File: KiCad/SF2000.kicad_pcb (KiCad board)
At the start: 4 copper layers, 111.5 x 83.9 mm, 104 parts, among them J1 Conn_2Rows-86Pins_even_odd, J10 Conn_02x01, J11 Conn_02x01, J2 Conn_01x02, J20 Conn_02x11_Odd_Even, J3 Conn_02x05_Odd_Even, J4 Conn_02x01, J5 Conn_01x01, J6 Micro_SD_Card_Socket, J7 Conn_02x01, J8 Conn_02x01, J9 Conn_02x01, Q1 MMBT3904, Q2 MMBT3906, U1 LM1117-3.3, U10 IS61WV20488FBLL-10TLI, U11 IS61WV20488FBLL-10TLI, U12 IS61WV20488FBLL-10TLI, U13 IS61WV20488FBLL-10TLI, U14 SST39LF040, U15 SST39LF802C, U16 74AHCT3G14, U2 ABLIC S-1132B43-M5T1U, U20 AT25SF081B-SSH, U3 TLV74312PDBV, U4 SN74CBT16211, U5 SN74CBT16211, U6 SN74CBT16211, U7 SN74AUP1T87DCKR, U8 T8Q144C3, U9 68000D, X1 Oscillator_7.0x5.0mm

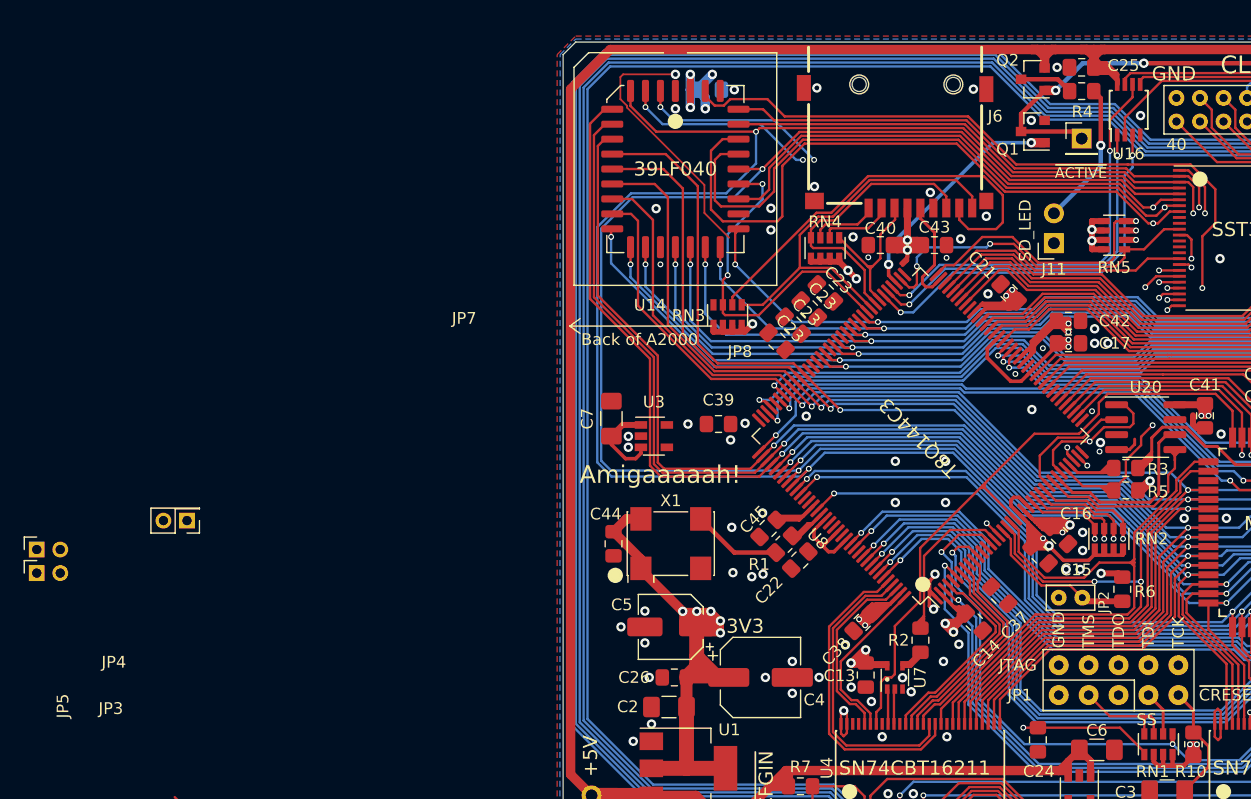
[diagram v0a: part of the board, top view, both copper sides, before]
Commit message: Fixed driver bank select jumper for ROM at U14, pulled-up by vacant resistor in RN3
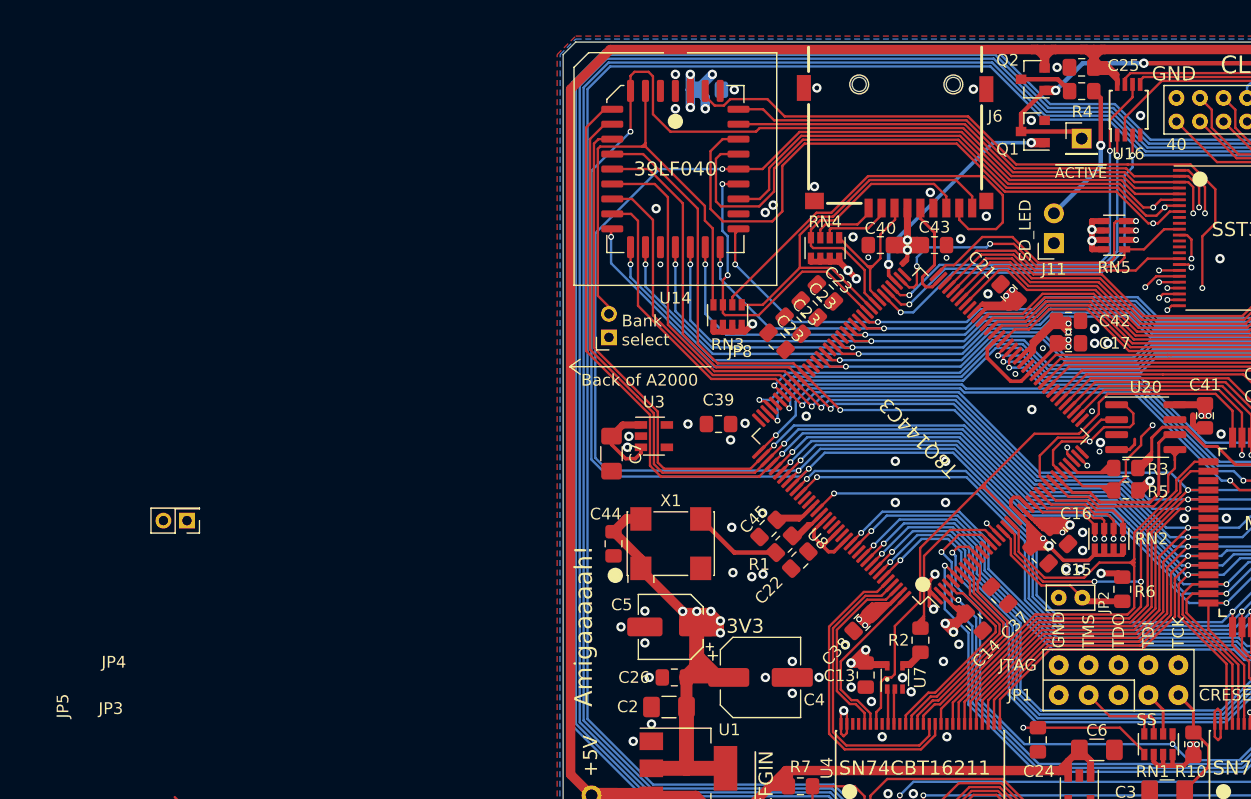
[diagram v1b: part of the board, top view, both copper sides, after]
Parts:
- removed J10: Conn_02x01, Connector_PinHeader_2.00mm:PinHeader_2x01_P2.00mm_Vertical
- moved J9 51.8 mm to (101.5, 84.2), turned to 90 degrees
- moved C7 2.98 mm to (101.8, 94.1), turned to 90 degrees
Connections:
- J9 pad 2: JP7 -> ROM_B1
- RN3 pad 4: Net-(RN3-Pad4) -> ROM_B1
- U14 pad 2: ROM_B2 -> GND
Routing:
- net ROM_B1: track 16.7 -> 39.8 mm, vias 2 -> 0
- net GND: track 152.6 -> 130.4 mm
- net ROM_B2: track 16.4 -> 0.00 mm, vias 2 -> 0
- net A13_3V3: track 253.1 -> 251.0 mm
- net ROM_OE: track 29.5 -> 28.0 mm
- net A12_3V3: track 236.4 -> 235.2 mm
- net A6_3V3: track 210.1 -> 211.2 mm
- net A5_3V3: track 192.5 -> 191.3 mm
- net A4_3V3: track 189.6 -> 188.9 mm
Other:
- board text added: "Bank select"
- board text removed: "JP7"

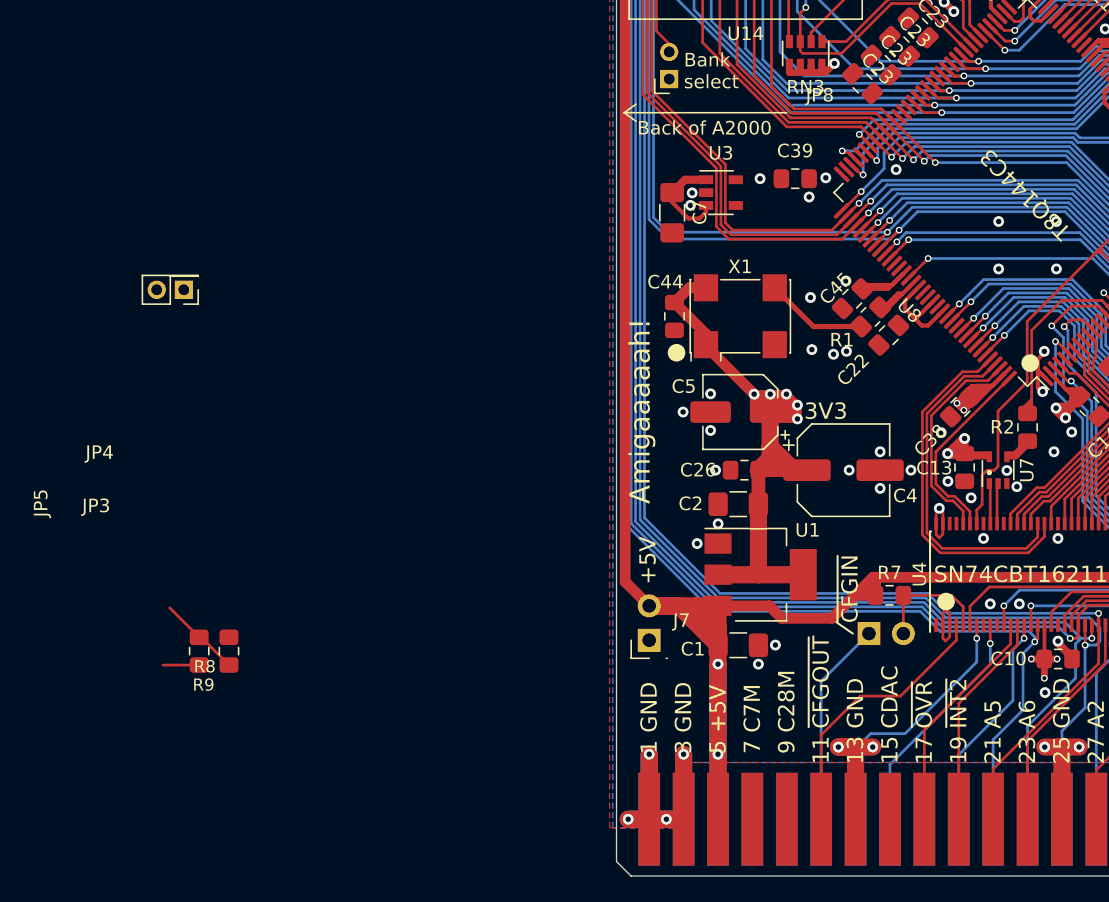
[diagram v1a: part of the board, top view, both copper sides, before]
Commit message: Swap position of BOSS and INT2 signal in FPGA and level shifters
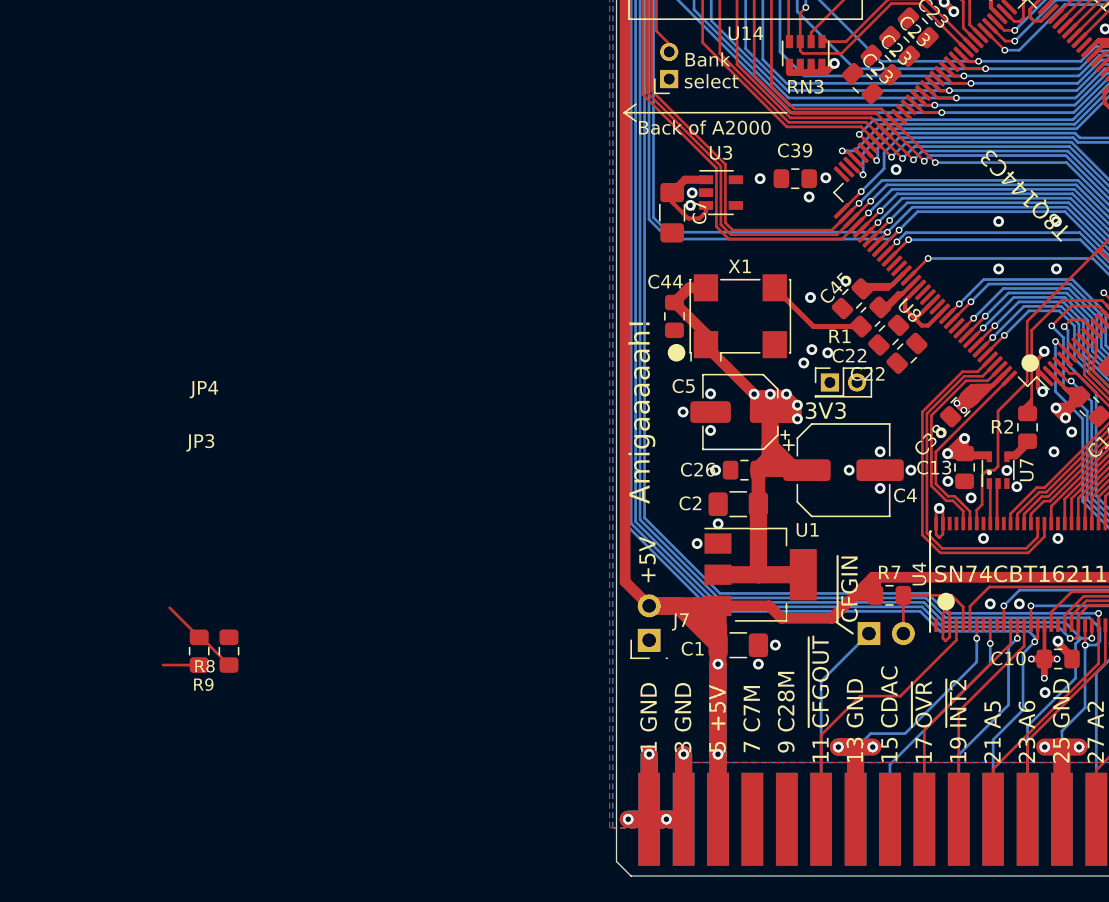
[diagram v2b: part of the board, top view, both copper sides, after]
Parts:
- added C22: 0.1uF, Capacitor_SMD:C_0805_2012Metric_Pad1.15x1.40mm_HandSolder, F.Cu at (119.1, 104.5)
- moved J8 48.2 mm to (113.4, 106.6), turned to 0 degrees
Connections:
- U4 pad 13: INT2 -> BOSS
- U4 pad 14: BOSS -> INT2
- U4 pad 42: BOSS_3V3 -> INT2_3V3
- U4 pad 43: INT2_3V3 -> BOSS_3V3
- U8 pad 10: BOSS_3V3 -> INT2_3V3
- U8 pad 8: INT2_3V3 -> BOSS_3V3
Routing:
- net INT2_3V3: track 17.8 -> 18.5 mm
- net BOSS_3V3: track 18.5 -> 17.8 mm
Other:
- board text removed: "I/O"
- board text removed: "JP5"
- board text removed: "JP8"
- board text removed: "MISO"
- board text removed: "MOSI"
- board text removed: "SCK"
- board text removed: "~CS"
- board text removed: "~INT"
- board text removed: "~RST"

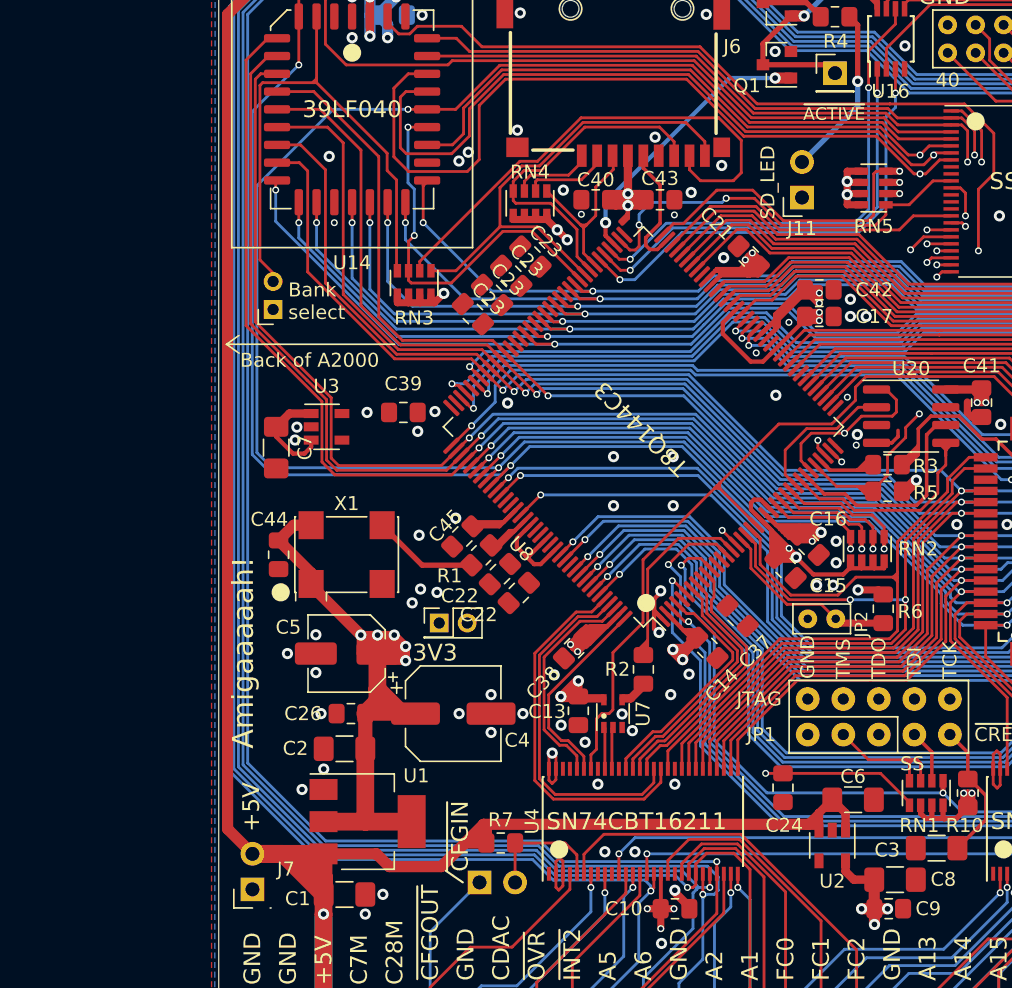
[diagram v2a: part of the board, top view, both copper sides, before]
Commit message: Remove INT6_3V3 signal and relocate JP2 to use this pin instead
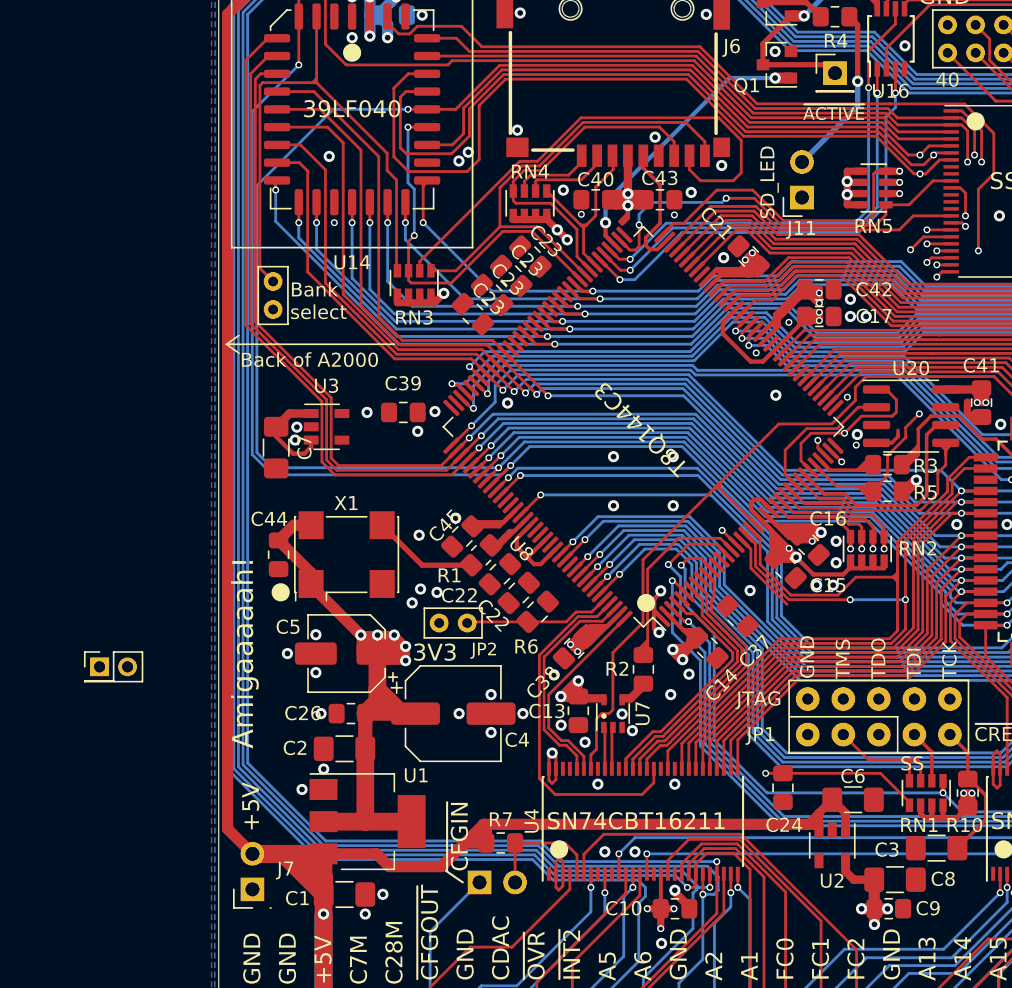
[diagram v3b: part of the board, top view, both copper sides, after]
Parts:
- moved J4 26.3 mm to (113.4, 106.6)
- moved R6 24.7 mm to (120.4, 105.8), turned to 225 degrees
- moved J8 24.5 mm to (89.1, 109.7)
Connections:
- J8 pad 2: JP6 -> JP4
- U4 pad 16: INT6 -> GND
- U4 pad 40: INT6_3V3 -> Net-(U4-Pad40)
- U8 pad 140: INT6_3V3 -> JP2
- U8 pad 17: JP2 -> JP4
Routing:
- net INT6_3V3: track 26.7 -> 0.00 mm
- net JP4: track 0.00 -> 5.97 mm
- net JP2: track 13.4 -> 10.5 mm
- net INT6: track 188.8 -> 186.8 mm, vias 1 -> 0
- net 3V3: track 290.9 -> 289.0 mm

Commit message: placement of JP3 and JP4
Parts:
- added J10: Conn_02x01, Connector_PinHeader_2.00mm:PinHeader_2x01_P2.00mm_Vertical, F.Cu at (145.0, 106.6)
- moved J8 56.1 mm to (145.0, 104.6), turned to 180 degrees
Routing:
- net JP4: track 5.97 -> 11.8 mm
- net TDO: track 25.3 -> 24.2 mm
- net TMS: track 20.3 -> 19.7 mm
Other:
- board text removed: "3V3"

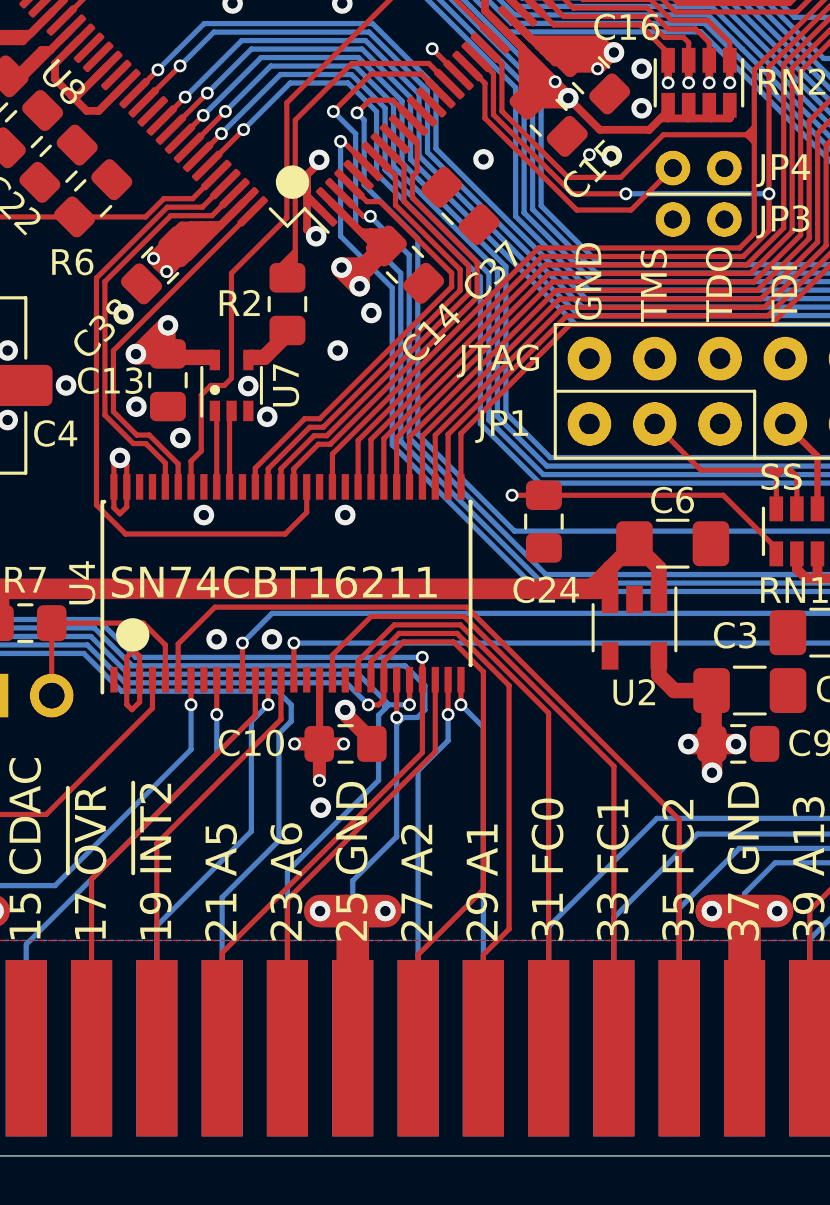
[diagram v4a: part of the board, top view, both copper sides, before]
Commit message: Remove INT2_3V3 pin and instead use it for JP3
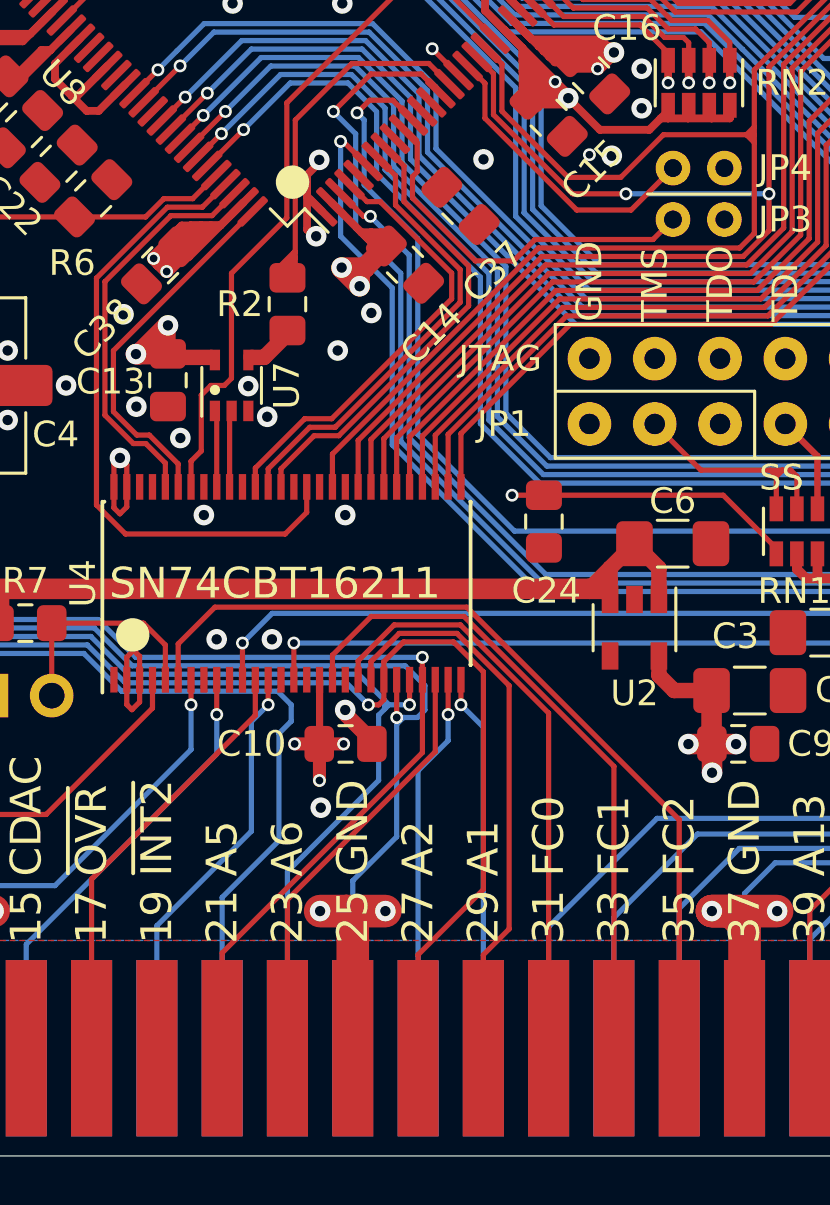
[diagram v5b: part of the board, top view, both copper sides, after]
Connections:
- J10 pad 1: Net-(J10-Pad1) -> GND
- J10 pad 2: Net-(J10-Pad2) -> JP3
- U4 pad 14: INT2 -> GND
- U4 pad 42: INT2_3V3 -> Net-(U4-Pad42)
- U8 pad 10: INT2_3V3 -> JP3
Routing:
- net INT2_3V3: track 18.5 -> 0.00 mm
- net INT2: track 16.3 -> 0.00 mm
- net JP3: track 0.00 -> 14.8 mm
